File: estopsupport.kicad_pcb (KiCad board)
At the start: 2 copper layers, 2 x 2 mm, 32 parts, among them J1 Barrier Block 1x3, J3 Dupont 1x2, J4 Dupont 1x2, J5 Dupont 2x4, J6 Dupont 1x2, K1 Relay_SPST-NO, Q1 PN2222A, U1 PC817, U2 BTS6163D

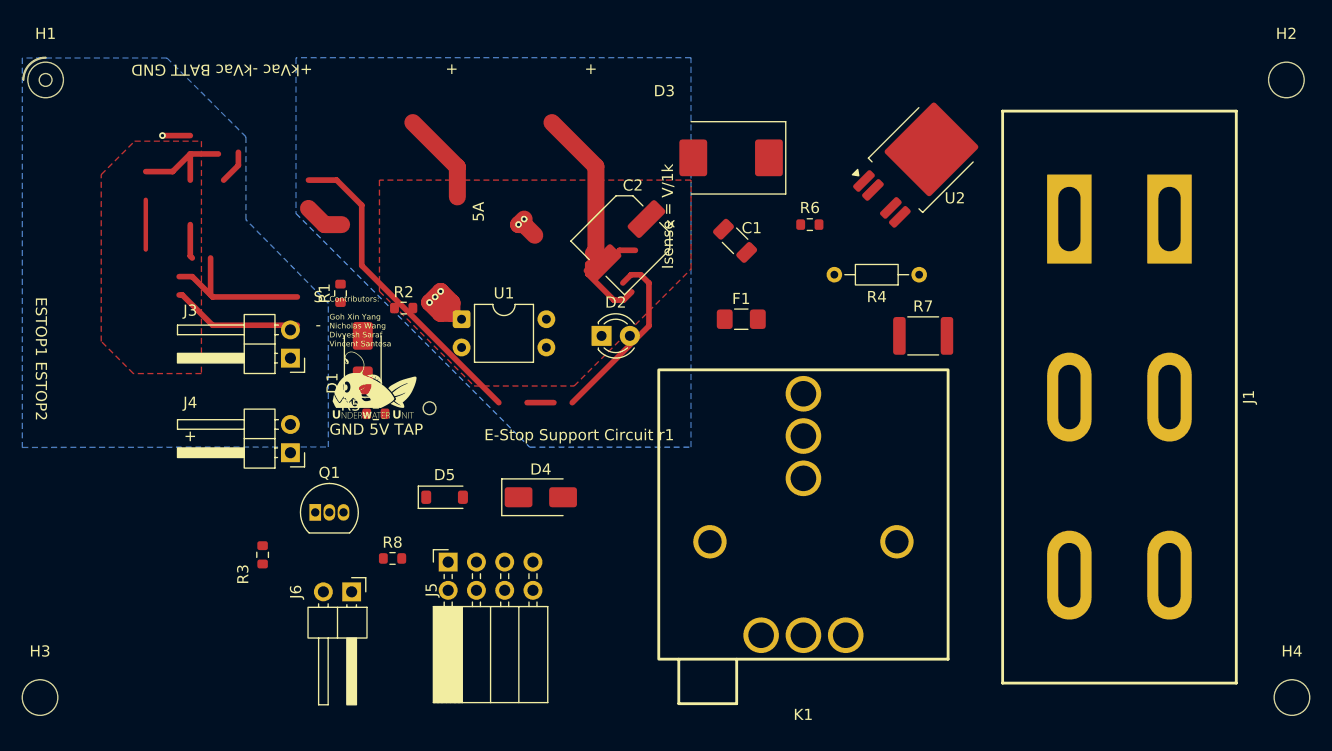
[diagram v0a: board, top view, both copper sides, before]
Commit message: feat: simplified circuit with 2n7004 mosfet, routed power side - awaiting gpio capability confirmation
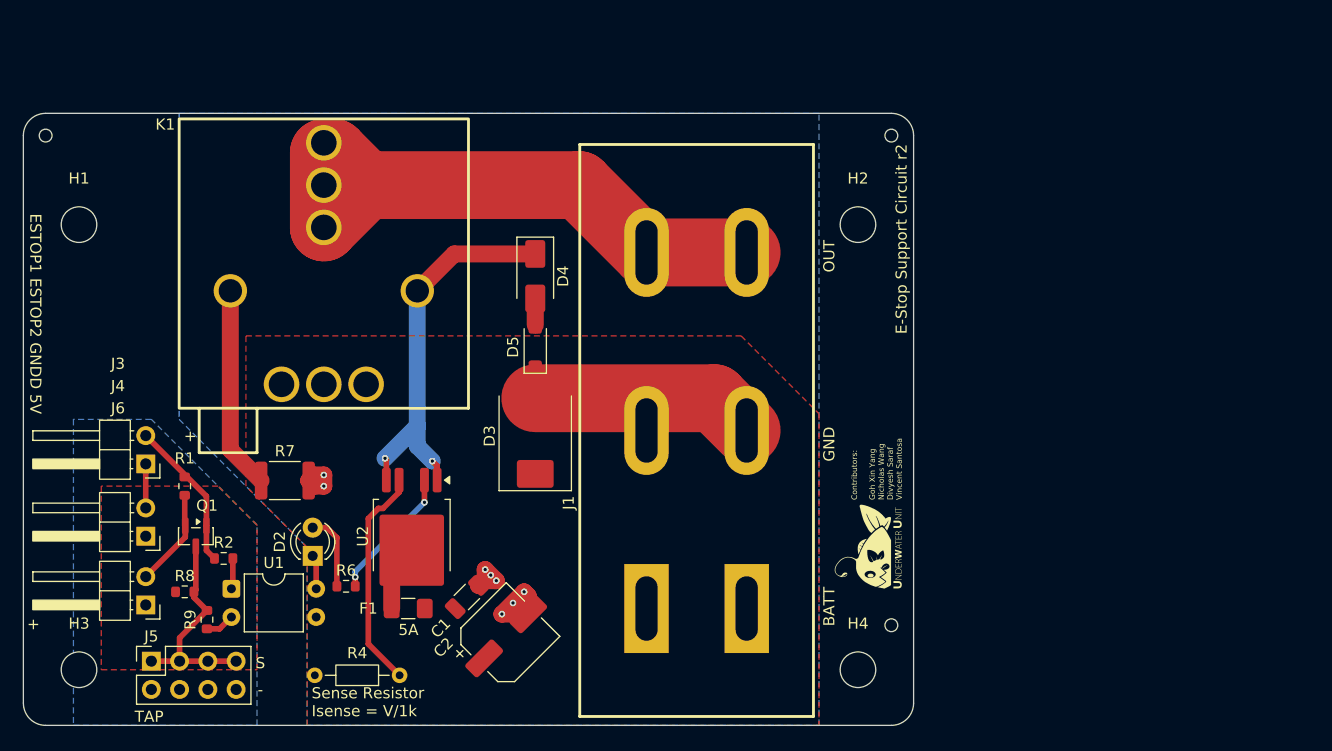
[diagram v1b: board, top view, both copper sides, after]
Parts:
- removed D1: 1N4007, Diode_SMD:D_SMA
- removed R3: 10k, Resistor_SMD:R_0603_1608Metric
- removed R5: 4.3k, Resistor_SMD:R_0603_1608Metric
- added R9: 10k, Resistor_SMD:R_0603_1608Metric, F.Cu at (51.5, 81.8)
- added REF**: ToolingHole_1.152mm, MountingHole:ToolingHole_1.152mm, F.Cu at (113.0, 38.3)
- J5: footprint Connector_PinSocket_2.54mm:PinSocket_2x04_P2.54mm_Horizontal -> Connector_PinSocket_2.54mm:PinSocket_2x04_P2.54mm_Vertical
- K1: value Relay_SPST-NO -> QLRELAY JQX-V7H 012-1HP; footprint EasyEDA_Lib:RELAY-TH_JQX-V7H-012-1HP -> easyeda-modified:RELAY-TH_JQX-V7H-012-1HP
- Q1: value PN2222A -> 2N7002; footprint Package_TO_SOT_THT:TO-92_Inline -> Package_TO_SOT_SMD:SOT-23
- R8: value 1k -> 4.3k
- moved R4 59.0 mm to (68.8, 86.8)
- moved R7 58.8 mm to (58.5, 69.3)
- moved U2 57.0 mm to (69.9, 74.3), turned to -90 degrees
- moved R6 52.8 mm to (64.0, 78.8)
- moved K1 48.6 mm to (62.0, 49.8)
- moved G*** 46.8 mm to (111.0, 75.3), turned to 90 degrees
- moved REF** 45.9 mm to (113.0, 82.3)
- moved H2 40.6 mm to (110.0, 46.3)
- moved C1 40.1 mm to (74.9, 79.7), turned to 45 degrees
- moved F1 39.6 mm to (69.6, 80.8)
- moved H4 39.1 mm to (110.0, 86.3)
- moved J1 38.1 mm to (95.5, 64.8), turned to 90 degrees
- moved C2 37.1 mm to (78.4, 83.3), turned to 45 degrees
- moved D2 32.6 mm to (61.0, 76.0), turned to 90 degrees
- moved U1 31.9 mm to (53.7, 79.0)
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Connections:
- net Net-(J5-Pin_1) renamed TAP_SIGNAL
- J3 pad 2: Net-(D1-A) -> Net-(J3-Pin_2)
- Q1 pad 1: GNDD -> Net-(J3-Pin_2)
- Q1 pad 2: Net-(Q1-B) -> GNDD
- R1 pad 1: Net-(D1-A) -> Net-(J3-Pin_2)
- R2 pad 1: Net-(D1-A) -> Net-(J3-Pin_2)
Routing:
- net Net-(J1-Pin_3): track 0.00 -> 57.6 mm
- net Net-(D4-K): track 0.00 -> 35.8 mm, vias 0 -> 2
- net Net-(D2-K): track 28.6 -> 3.09 mm
- net Net-(D1-A): track 21.3 -> 0.00 mm
- net Net-(U2-IS): track 0.00 -> 20.1 mm
- net TAP_SIGNAL: track 0.00 -> 19.5 mm
- net Net-(K1-PadA2): track 0.00 -> 18.2 mm
- net Net-(Q1-B): track 14.7 -> 0.00 mm
- net Net-(J3-Pin_2): track 0.00 -> 13.6 mm
- net Net-(U2-IN): track 0.00 -> 12.1 mm, vias 0 -> 2
- net Net-(D2-A): track 19.0 -> 6.92 mm
- net GNDD: track 2.50 -> 11.4 mm, vias 1 -> 0
- net Net-(J1-Pin_1): track 8.34 -> 0.00 mm
- net Net-(R2-Pad2): track 9.29 -> 2.78 mm
- net GND: track 30.1 -> 36.6 mm, vias 5 -> 8
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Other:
- board size 2 x 2 mm -> 80 x 55 mm
- board text added: "BATT"
- board text added: "ESTOP1 ESTOP2 GNDD 5V"
- board text added: "GND"
- board text added: "OUT"
- board text added: "Sense Resistor Isense = V/1k"
- board text added: "TAP"
- board text removed: "+kVac -kVac BATT GND"
- board text removed: "ESTOP1 ESTOP2"
- board text removed: "GND 5V TAP"
- board text removed: "Isense = V/1k"

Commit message: chore: geographical reannotate
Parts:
- renumbered D4 to D1, D5 to D2, D2 to D4, J3 to J2, J4 to J3, J6 to J4, R7 to R1, R1 to R2, R2 to R3, R6 to R4, R8 to R5, R9 to R6, R4 to R7, U2 to U1, U1 to U2

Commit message: chore: move relay a bit to the right
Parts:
- moved K1 1.50 mm to (63.5, 49.8)
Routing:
- net Net-(J1-Pin_3): track 57.6 -> 56.1 mm
- net Net-(D1-K): track 35.8 -> 35.0 mm
- net Net-(K1-PadA2): track 18.2 -> 17.6 mm

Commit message: layout rework
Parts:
- C1, D1, D2, R1: moved to B.Cu
- moved D3 33.7 mm to (52.8, 46.9)
- moved D2 16.3 mm to (65.0, 54.3), turned to -45 degrees
- moved R1 16.1 mm to (57.0, 53.3), turned to 90 degrees
- moved D1 10.4 mm to (72.0, 56.0), turned to 180 degrees
- moved D4 10.3 mm to (59.7, 86.3), turned to 0 degrees
- moved R4 7.82 mm to (68.6, 85.1)
- moved K1 7.13 mm to (69.7, 53.3)
- moved C1 7.06 mm to (73.2, 72.9), turned to -90 degrees
- moved C2 6.45 mm to (79.2, 76.9), turned to -90 degrees
- moved U1 6.25 mm to (68.8, 80.4), turned to 180 degrees
- moved F1 6.16 mm to (67.8, 74.9), turned to 180 degrees
- moved R7 5.45 mm to (74.0, 85.1), turned to 0 degrees
- moved J1 1.80 mm to (94.0, 63.8)
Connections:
- J1 pad 1: +BATT -> GND
- J1 pad 2: GND -> +BATT
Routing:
- net Net-(D1-K): track 35.0 -> 92.3 mm, vias 2 -> 3
- net Net-(J1-Pin_3): track 56.1 -> 0.00 mm
- net +BATT: track 0.00 -> 47.2 mm
- net GND: track 36.7 -> 20.3 mm, vias 8 -> 5
- net Net-(K1-PadA2): track 17.6 -> 4.38 mm
- net Net-(U1-IS): track 20.1 -> 9.40 mm
- net Net-(D4-K): track 3.09 -> 9.29 mm
- net Net-(U1-IN): track 12.1 -> 6.66 mm, vias 2 -> 0
- net Net-(D1-A): track 2.40 -> 4.07 mm
- net Net-(D4-A): track 6.92 -> 6.03 mm
- added copper zone on B.Cu, net +BATT
- added copper zone on B.Cu, net Net-(J1-Pin_3)
- added copper zone on F.Cu, net Net-(J1-Pin_3)

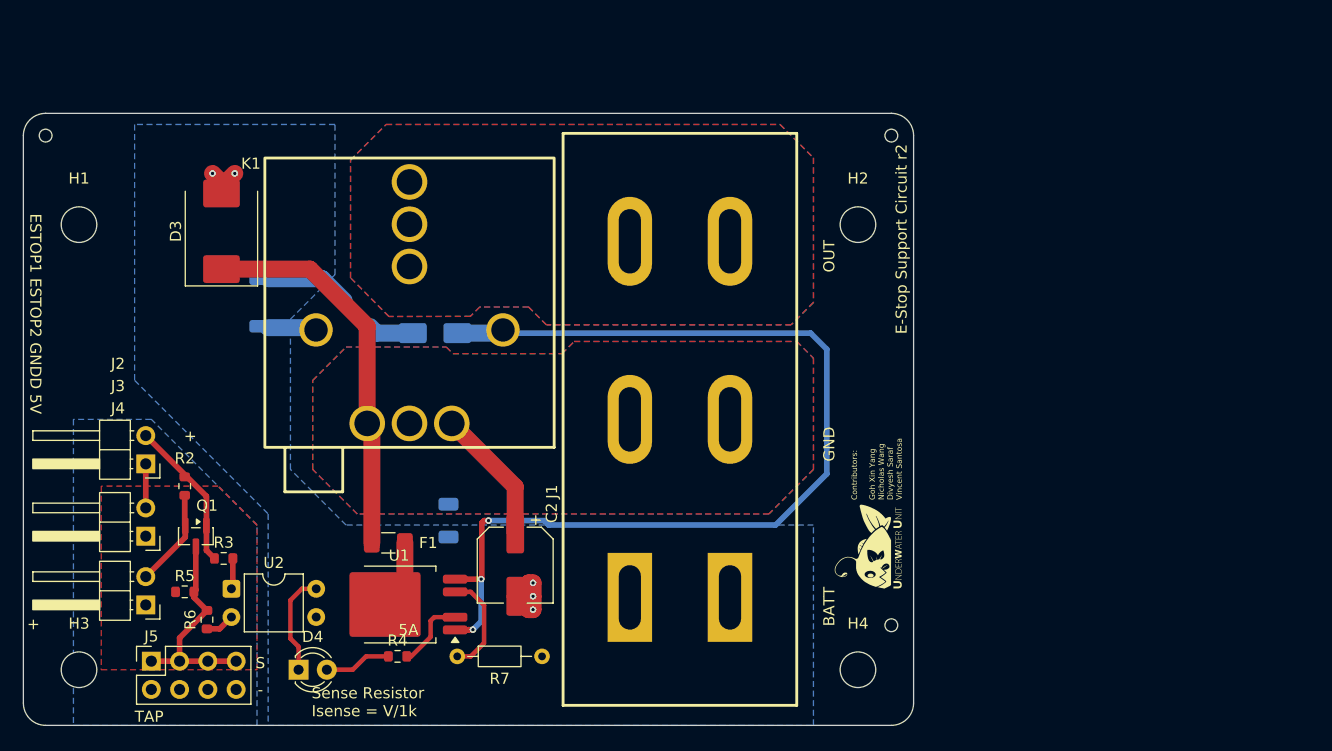
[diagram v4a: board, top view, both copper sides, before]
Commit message: feat: change to 4 layers, put everything on the top layer so that it can be assembled by jlcpcb cheaply
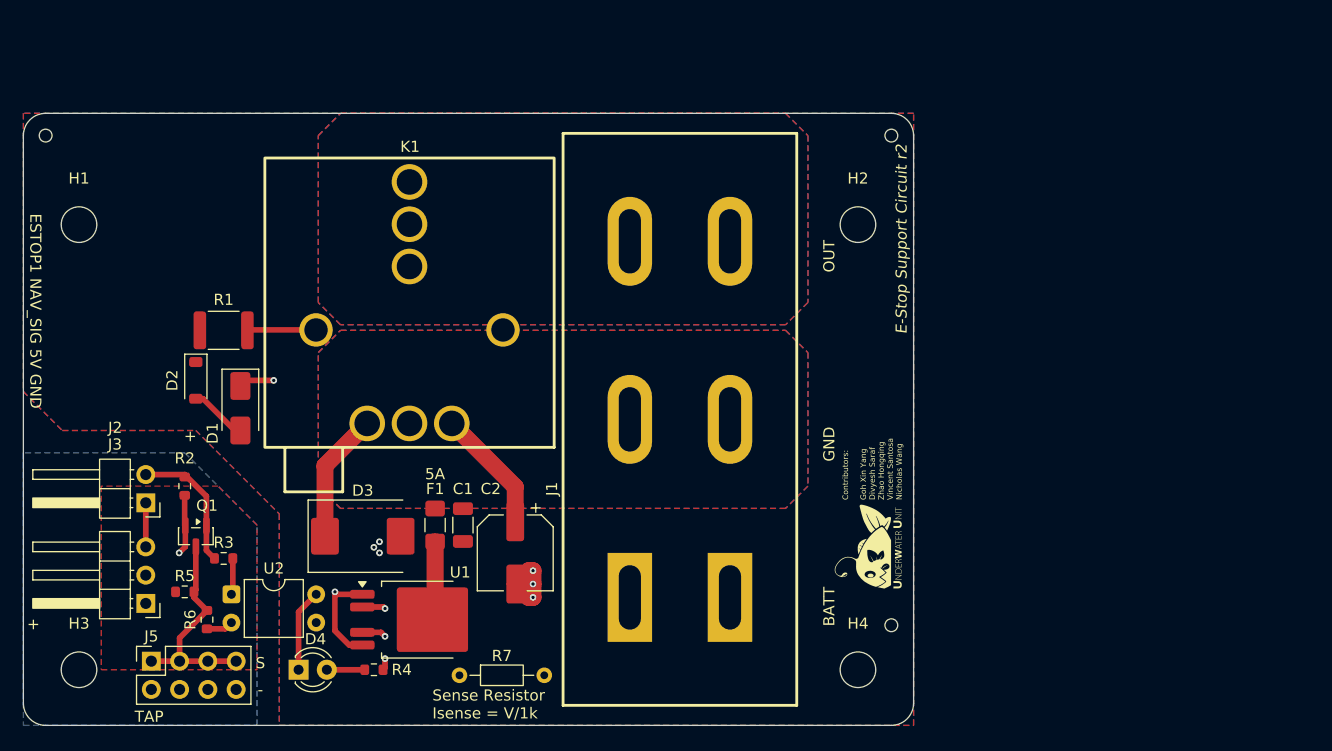
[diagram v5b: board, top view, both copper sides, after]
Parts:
- removed J4: Dupont 1x2, Connector_PinHeader_2.54mm:PinHeader_1x02_P2.54mm_Horizontal
- C1, D1, D2, R1: moved to F.Cu
- F1: value 5A -> 0.5A
- J3: value Dupont 1x2 -> Dupont 1x3; footprint Connector_PinHeader_2.54mm:PinHeader_1x02_P2.54mm_Horizontal -> Connector_PinHeader_2.54mm:PinHeader_1x03_P2.54mm_Horizontal
- Q1: value 2N7002 -> AO3400A
- moved D3 30.2 mm to (65.5, 74.3), turned to 0 degrees
- moved D1 18.8 mm to (54.5, 62.8), turned to -90 degrees
- moved D2 15.7 mm to (50.5, 60.3), turned to -90 degrees
- moved J3 6.04 mm to (46.0, 80.3)
- moved R1 4.72 mm to (53.0, 55.8), turned to 180 degrees
- moved F1 4.49 mm to (72.0, 73.3), turned to 90 degrees
- moved J2 3.50 mm to (46.0, 71.3)
- moved R4 2.44 mm to (66.5, 86.3)
- moved U1 2.21 mm to (70.5, 81.8), turned to 0 degrees
- moved R7 1.71 mm to (74.2, 86.8)
- moved C1 1.36 mm to (74.5, 73.3)
- moved C2 1.10 mm to (79.2, 75.8)
- moved U2 0.50 mm to (53.7, 79.5)
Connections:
- net Net-(J1-Pin_3) renamed POWER_OUT
- J3 pad 1: +5V -> GNDD
- J3 pad 2: Net-(J2-Pin_1) -> +5V
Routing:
- net Net-(D1-K): track 92.3 -> 56.7 mm, vias 3 -> 2
- net +BATT: track 47.2 -> 22.9 mm
- net GND: track 20.3 -> 8.19 mm, vias 5 -> 6
- net GNDD: track 11.4 -> 7.85 mm, vias 0 -> 1
- net Net-(D4-A): track 6.03 -> 3.40 mm
- net Net-(D4-K): track 9.29 -> 7.43 mm
- net Net-(U1-IN): track 6.66 -> 8.50 mm, vias 0 -> 2
- net Net-(K1-PadA2): track 4.38 -> 6.09 mm
- net Net-(J2-Pin_2): track 13.6 -> 12.1 mm
- net Net-(D1-A): track 4.07 -> 5.39 mm
- net Net-(R3-Pad2): track 2.78 -> 3.78 mm
- net Net-(U1-IS): track 9.40 -> 10.3 mm, vias 0 -> 1
- net Net-(U1-Vbb): track 6.28 -> 7.11 mm
- added copper zone on In1.Cu, net +BATT
- added copper zone on In2.Cu, net +BATT
- added copper zone on F.Cu, net GND
- added copper zone on In1.Cu, net GND
- added copper zone on In2.Cu, net GND
- added copper zone on In1.Cu, net POWER_OUT
- added copper zone on In2.Cu, net POWER_OUT
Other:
- copper layers 2 -> 4
- board text added: "Contributors: Goh Xin Yang Divyesh Saraf Zhao Hongqing Vincent Santosa Nicholas Wang"
- board text added: "ESTOP1 NAV_SIG 5V GND"
- board text removed: "Contributors: Goh Xin Yang Nicholas Wang Divyesh Saraf Vincent Santosa"
- board text removed: "ESTOP1 ESTOP2 GNDD 5V"

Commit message: reverse fuse protection, silkscreen adjust and check for production
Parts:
- added R8: 33, Resistor_SMD:R_1812_4532Metric, F.Cu at (53.0, 50.8)
- R1: value 15 -> 33
- moved C1 1.62 mm to (74.4, 74.9)
- turned D3 to 180 degrees
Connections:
- C1 pad 1: +BATT -> Net-(D3-K)
- C2 pad 1: +BATT -> Net-(D3-K)
- D3 pad 1: +BATT -> Net-(D3-K)
- F1 pad 1: Net-(U1-Vbb) -> Net-(D3-K)
- U1 pad 3: Net-(U1-Vbb) -> Net-(D3-K)
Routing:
- net +BATT: track 22.9 -> 0.00 mm
- net Net-(D3-K): track 0.00 -> 18.4 mm
- net Net-(U1-Vbb): track 7.11 -> 0.00 mm
- net Net-(K1-PadA2): track 6.09 -> 11.2 mm
- net Net-(D1-K): track 56.7 -> 55.6 mm
- added copper zone on In1.Cu, net GNDD
- added copper zone on In2.Cu, net GNDD
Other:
- board text added: "0.5A"
- board text removed: "5A"
